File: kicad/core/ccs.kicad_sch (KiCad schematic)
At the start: 8 parts, among them Q1 IRLZ44N, U3 OPA192, U4 TL431LP

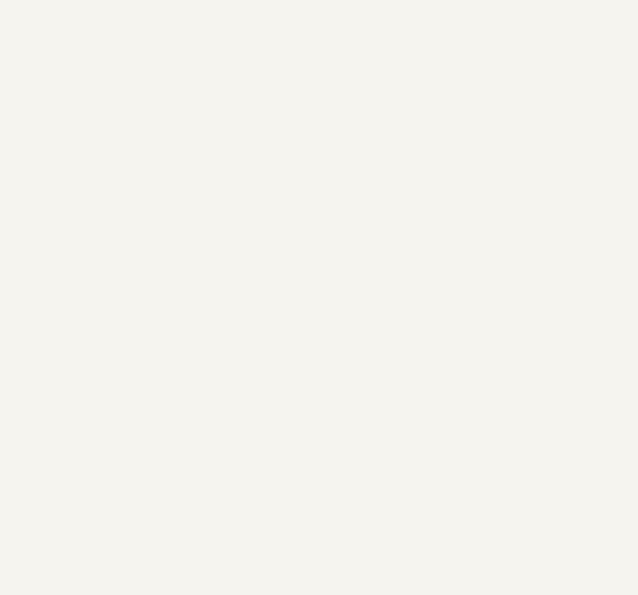
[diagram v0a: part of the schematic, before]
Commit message: Prove the 2×2 access cycle from the address pins through decode, drive, and the sense latch.
Three current sinks, the diode matrix, and drive groups 0--7 are on the schematic. The four-core decks are the gate; weave inductance is still an open input.
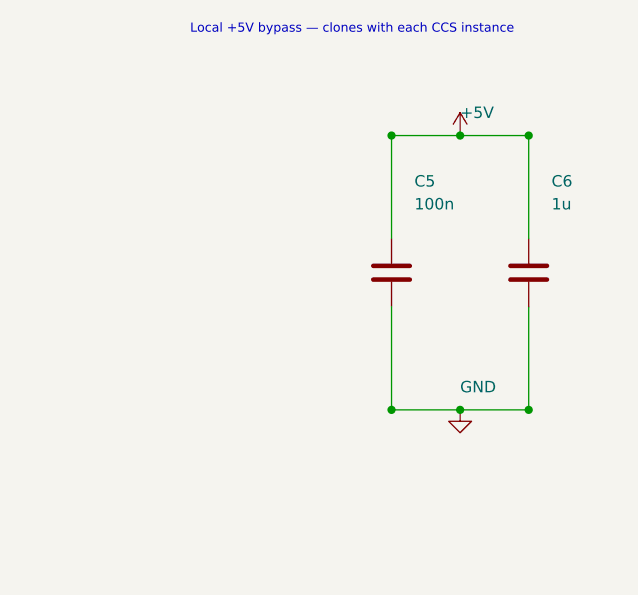
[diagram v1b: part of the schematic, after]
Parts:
- added C5: 100n, Capacitor_SMD:C_0805_2012Metric, symbol Device:C
- added C6: 1u, Capacitor_SMD:C_0805_2012Metric, symbol Device:C
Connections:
- net +5V: now also C5.1, C6.1
- net GND: now also C5.2, C6.2
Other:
- note added: "Local +5V bypass — clones with each CCS instance"
